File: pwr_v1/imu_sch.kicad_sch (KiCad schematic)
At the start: 5 parts, among them U4 LSM6DSLTR

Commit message: Schematic updated
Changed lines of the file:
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@@
+	)
+	(junction
+		(at 128.27 38.1)
+		(diameter 0)
+		(color 0 0 0 0)
 	)
 	(junction
@@
 	(junction
 		(at 67.31 55.88)
+		(diameter 0)
+		(color 0 0 0 0)
+	)
+	(junction
+		(at 53.34 55.88)
 		(diameter 0)
 		(color 0 0 0 0)
@@
 	)
 	(symbol
+		(lib_id "power:PWR_FLAG")
+		(at 53.34 55.88 90)
+		(unit 1)
+		(exclude_from_sim no)
+		(in_bom yes)
+		(on_board yes)
+		(dnp no)
+		(fields_autoplaced yes)
+		(property "Reference" "#FLG06"
+			(at 51.435 55.88 0)
+			(effects
+				(font
+					(size 1.27 1.27)
+				)
+				(hide yes)
+			)
+		)
+		(property "Value" "PWR_FLAG"
+			(at 49.53 55.8799 90)
+			(effects
+				(font
+					(size 1.27 1.27)
+				)
+				(justify left)
+			)
+		)
+		(property "Footprint" ""
+			(at 53.34 55.88 0)
+			(effects
+				(font
+					(size 1.27 1.27)
+				)
+				(hide yes)
+			)
+		)
+		(property "Datasheet" "~"
+			(at 53.34 55.88 0)
+			(effects
+				(font
+					(size 1.27 1.27)
+				)
+				(hide yes)
+			)
+		)
+		(property "Description" "Special symbol for telling ERC where power comes from"
+			(at 53.34 55.88 0)
+			(effects
+				(font
+					(size 1.27 1.27)
+				)
+				(hide yes)
+			)
+		)
+		(pin "1"
+		)
+		(instances
+			(project "pwr_v1"
+				(path "/42eee4f9-ea65-4e89-8296-df9554a24009/b4721251-ca72-44ff-8b38-c2b8be0e5ec8"
+					(reference "#FLG06")
+					(unit 1)
+				)
+			)
+		)
+	)
+	(symbol
 		(lib_id "imu:LSM6DSLTR")
 		(at 69.85 53.34 0)
@@
 					(unit 1)
 				)
+			)
+		)
+	)
+	(symbol
+		(lib_id "power:PWR_FLAG")
+		(at 128.27 38.1 270)
+		(unit 1)
+		(exclude_from_sim no)
+		(in_bom yes)
+		(on_board yes)
+		(dnp no)
+		(fields_autoplaced yes)
+		(property "Reference" "#FLG05"
+			(at 130.175 38.1 0)
+			(effects
+				(font
+					(size 1.27 1.27)
+				)
+				(hide yes)
+			)
+		)
+		(property "Value" "PWR_FLAG"
+			(at 132.08 38.0999 90)
+			(effects
+				(font
+					(size 1.27 1.27)
+				)
+				(justify left)
+			)
+		)
+		(property "Footprint" ""
+			(at 128.27 38.1 0)
+			(effects
+				(font
+					(size 1.27 1.27)
+				)
+				(hide yes)
+			)
+		)
+		(property "Datasheet" "~"
+			(at 128.27 38.1 0)
+			(effects
+				(font
+					(size 1.27 1.27)
+				)
+				(hide yes)
+			)
+		)
+		(property "Description" "Special symbol for telling ERC where power comes from"
+			(at 128.27 38.1 0)
+			(effects
+				(font
+					(size 1.27 1.27)
+				)
+				(hide yes)
+			)
+		)
+		(pin "1"
+		)
+		(instances
+			(project "pwr_v1"
+				(path "/42eee4f9-ea65-4e89-8296-df9554a24009/b4721251-ca72-44ff-8b38-c2b8be0e5ec8"
+					(reference "#FLG05")
+					(unit 1)
+				)

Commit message: Schematic and layout updated
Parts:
- C12, C13: footprint ceramic_cap:CAP_GRM155_MUR -> Capacitor_SMD:C_0402_1005Metric
- R2, R3: footprint res_1k:1206_PAN -> Resistor_SMD:R_0603_1608Metric
- U4: footprint (none) -> Package_LGA:LGA-14_3x2.5mm_P0.5mm_LayoutBorder3x4y

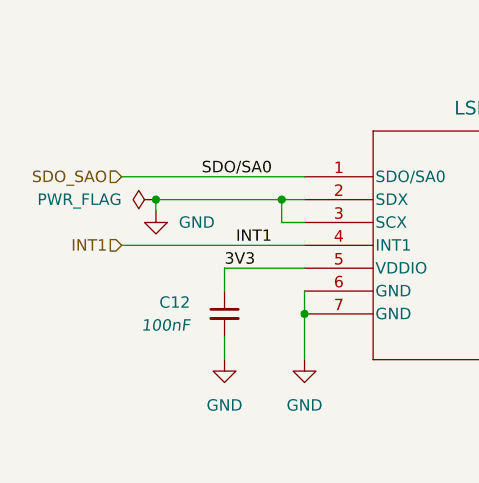
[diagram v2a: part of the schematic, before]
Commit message: Sch and Layout updated; Added batt sup ckt, placed and routed all motor drivers.
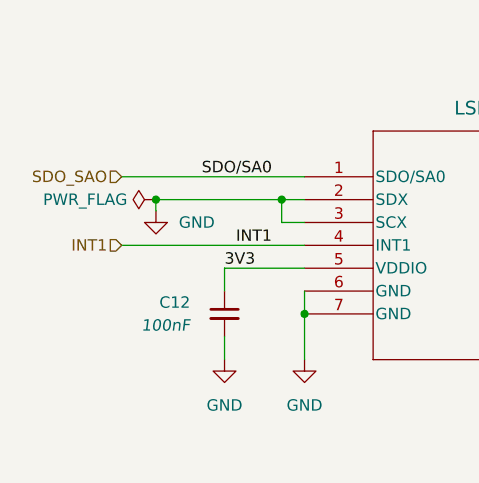
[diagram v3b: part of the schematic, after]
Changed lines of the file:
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@@
+	)
+	(junction
+		(at 53.34 55.88)
+		(diameter 0)
+		(color 0 0 0 0)
 	)
 	(junction
@@
 	(junction
 		(at 67.31 55.88)
-		(diameter 0)
-		(color 0 0 0 0)
-	)
-	(junction
-		(at 53.34 55.88)
 		(diameter 0)
 		(color 0 0 0 0)
@@
 	)
 	(symbol
-		(lib_id "power:PWR_FLAG")
-		(at 53.34 55.88 90)
-		(unit 1)
-		(exclude_from_sim no)
-		(in_bom yes)
-		(on_board yes)
-		(dnp no)
-		(fields_autoplaced yes)
-		(property "Reference" "#FLG06"
-			(at 51.435 55.88 0)
-			(effects
-				(font
-					(size 1.27 1.27)
-				)
-				(hide yes)
-			)
-		)
-		(property "Value" "PWR_FLAG"
-			(at 49.53 55.8799 90)
-			(effects
-				(font
-					(size 1.27 1.27)
-				)
-				(justify left)
-			)
-		)
-		(property "Footprint" ""
-			(at 53.34 55.88 0)
-			(effects
-				(font
-					(size 1.27 1.27)
-				)
-				(hide yes)
-			)
-		)
-		(property "Datasheet" "~"
-			(at 53.34 55.88 0)
-			(effects
-				(font
-					(size 1.27 1.27)
-				)
-				(hide yes)
-			)
-		)
-		(property "Description" "Special symbol for telling ERC where power comes from"
-			(at 53.34 55.88 0)
-			(effects
-				(font
-					(size 1.27 1.27)
-				)
-				(hide yes)
-			)
-		)
-		(pin "1"
-		)
-		(instances
-			(project "pwr_v1"
-				(path "/42eee4f9-ea65-4e89-8296-df9554a24009/b4721251-ca72-44ff-8b38-c2b8be0e5ec8"
-					(reference "#FLG06")
-					(unit 1)
-				)
-			)
-		)
-	)
-	(symbol
 		(lib_id "imu:LSM6DSLTR")
 		(at 69.85 53.34 0)
@@
 					(unit 1)
 				)
+			)
+		)
+	)
+	(symbol
+		(lib_id "power:PWR_FLAG")
+		(at 53.34 55.88 90)
+		(unit 1)
+		(exclude_from_sim no)
+		(in_bom yes)
+		(on_board yes)
+		(dnp no)
+		(fields_autoplaced yes)
+		(property "Reference" "#FLG04"
+			(at 51.435 55.88 0)
+			(effects
+				(font
+					(size 1.27 1.27)
+				)
+				(hide yes)
+			)
+		)
+		(property "Value" "PWR_FLAG"
+			(at 50.165 55.8799 90)
+			(effects
+				(font
+					(size 1.27 1.27)
+				)
+				(justify left)
+			)
+		)
+		(property "Footprint" ""
+			(at 53.34 55.88 0)
+			(effects
+				(font
+					(size 1.27 1.27)
+				)
+				(hide yes)
+			)
+		)
+		(property "Datasheet" "~"
+			(at 53.34 55.88 0)
+			(effects
+				(font
+					(size 1.27 1.27)
+				)
+				(hide yes)
+			)
+		)
+		(property "Description" "Special symbol for telling ERC where power comes from"
+			(at 53.34 55.88 0)
+			(effects
+				(font
+					(size 1.27 1.27)
+				)
+				(hide yes)
+			)
+		)
+		(pin "1"
+		)
+		(instances
+			(project "pwr_v1"
+				(path "/42eee4f9-ea65-4e89-8296-df9554a24009/b4721251-ca72-44ff-8b38-c2b8be0e5ec8"
+					(reference "#FLG04")
+					(unit 1)
+				)

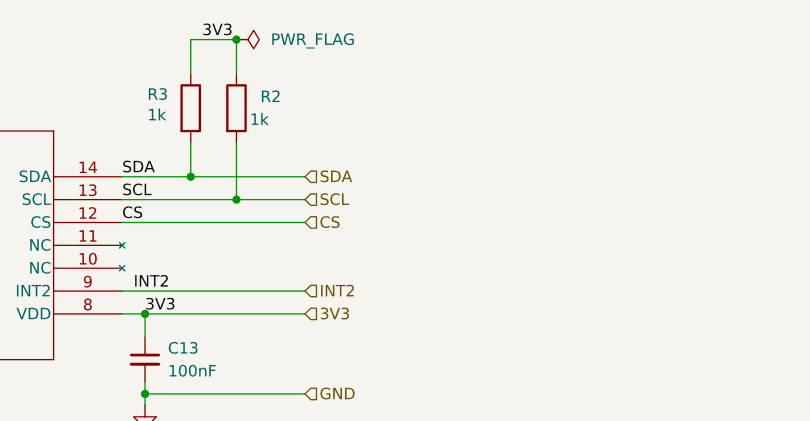
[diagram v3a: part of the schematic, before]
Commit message: Schematic updated; Layout updated; STM PinMappings file added
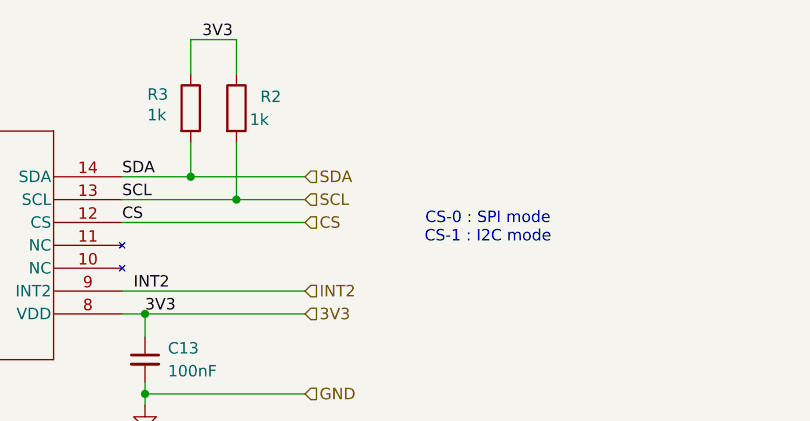
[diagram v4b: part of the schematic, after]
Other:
- note added: "CS-0 : SPI mode CS-1 : I2C mode"
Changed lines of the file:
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@@
-	)
-	(junction
-		(at 128.27 38.1)
-		(diameter 0)
-		(color 0 0 0 0)
 	)
 	(junction
@@
 			)
 			(justify left top)
+		)
+	)
+	(text "CS-0 : SPI mode\nCS-1 : I2C mode"
+		(exclude_from_sim no)
+		(at 156.21 59.055 0)
+		(effects
+			(font
+				(size 1.27 1.27)
+			)
 		)
 	)
@@
 					(unit 1)
 				)
-			)
-		)
-	)
-	(symbol
-		(lib_id "power:PWR_FLAG")
-		(at 128.27 38.1 270)
-		(unit 1)
-		(exclude_from_sim no)
-		(in_bom yes)
-		(on_board yes)
-		(dnp no)
-		(fields_autoplaced yes)
-		(property "Reference" "#FLG05"
-			(at 130.175 38.1 0)
-			(effects
-				(font
-					(size 1.27 1.27)
-				)
-				(hide yes)
-			)
-		)
-		(property "Value" "PWR_FLAG"
-			(at 132.08 38.0999 90)
-			(effects
-				(font
-					(size 1.27 1.27)
-				)
-				(justify left)
-			)
-		)
-		(property "Footprint" ""
-			(at 128.27 38.1 0)
-			(effects
-				(font
-					(size 1.27 1.27)
-				)
-				(hide yes)
-			)
-		)
-		(property "Datasheet" "~"
-			(at 128.27 38.1 0)
-			(effects
-				(font
-					(size 1.27 1.27)
-				)
-				(hide yes)
-			)
-		)
-		(property "Description" "Special symbol for telling ERC where power comes from"
-			(at 128.27 38.1 0)
-			(effects
-				(font
-					(size 1.27 1.27)
-				)
-				(hide yes)
-			)
-		)
-		(pin "1"
-		)
-		(instances
-			(project "pwr_v1"
-				(path "/42eee4f9-ea65-4e89-8296-df9554a24009/b4721251-ca72-44ff-8b38-c2b8be0e5ec8"
-					(reference "#FLG05")
-					(unit 1)
-				)

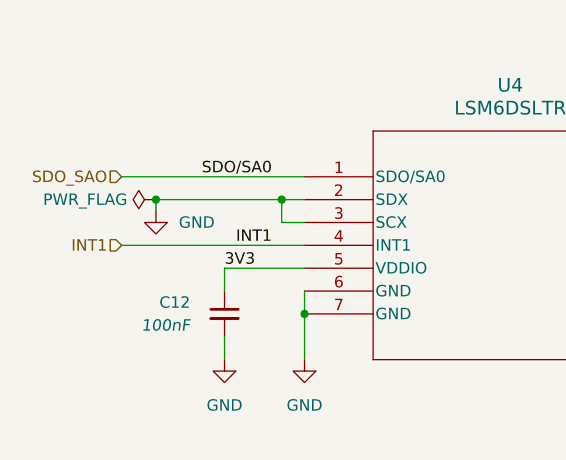
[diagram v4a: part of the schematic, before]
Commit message: Schematic and layout updated; Layout placement and routing completed
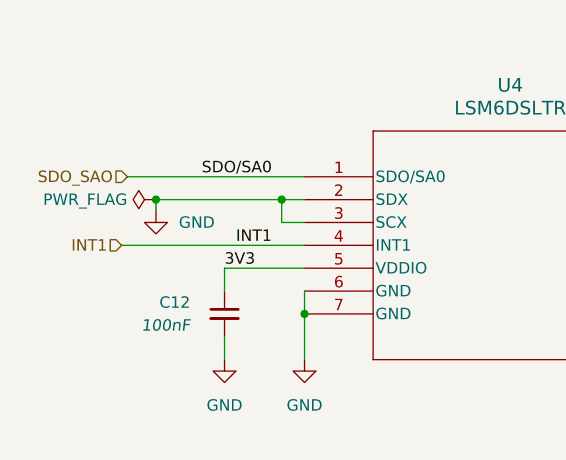
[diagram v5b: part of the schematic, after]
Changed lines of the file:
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@@
 	(wire
 		(pts
-			(xy 49.53 53.34) (xy 69.85 53.34)
+			(xy 50.165 53.34) (xy 69.85 53.34)
 		)
 		(stroke
@@
 	(hierarchical_label "SDO_SAO"
 		(shape input)
-		(at 49.53 53.34 180)
-		(fields_autoplaced yes)
-		(effects
+		(at 50.165 53.34 180)
+		(fields_autoplaced yes)
+		(effects

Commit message: Final PCB files sent for fab
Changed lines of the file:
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@@
 		)
 	)
-	(label "SDO{slash}SA0"
+	(label "SDO_SAO"
 		(at 58.42 53.34 0)
 		(fields_autoplaced yes)
@@
 	)
 	(symbol
+		(lib_name "GND_1")
 		(lib_id "power:GND")
 		(at 53.34 57.15 0)
@@
 			)
 		)
-		(property "Description" ""
+		(property "Description" "Power symbol creates a global label with name \"GND\" , ground"
 			(at 53.34 57.15 0)
 			(effects
@@
 			)
 		)
-		(property "Description" ""
+		(property "Description" "Power symbol creates a global label with name \"GND\" , ground"
 			(at 60.96 73.66 0)
 			(effects
@@
 			)
 		)
-		(property "Description" ""
+		(property "Description" "Power symbol creates a global label with name \"GND\" , ground"
 			(at 69.85 73.66 0)
 			(effects
@@
 			)
 		)
-		(property "Description" ""
+		(property "Description" "Power symbol creates a global label with name \"GND\" , ground"
 			(at 118.11 78.74 0)
 			(effects

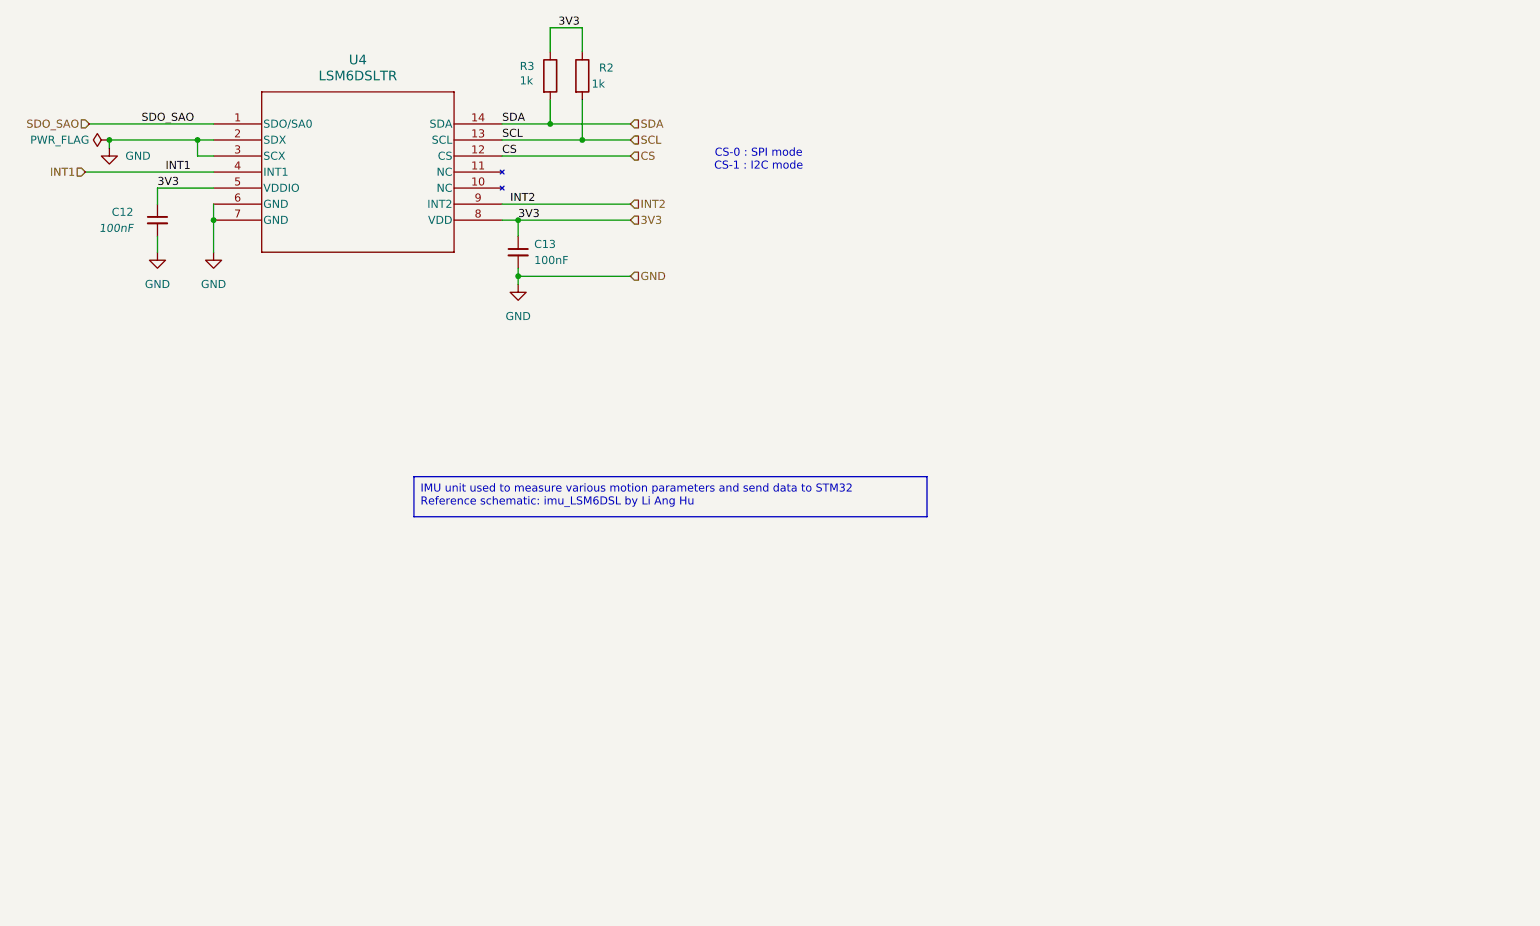
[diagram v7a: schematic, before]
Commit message: File structure enhanced.
Added uniform titleblocks and 3D renders for easier view, file cleanups.
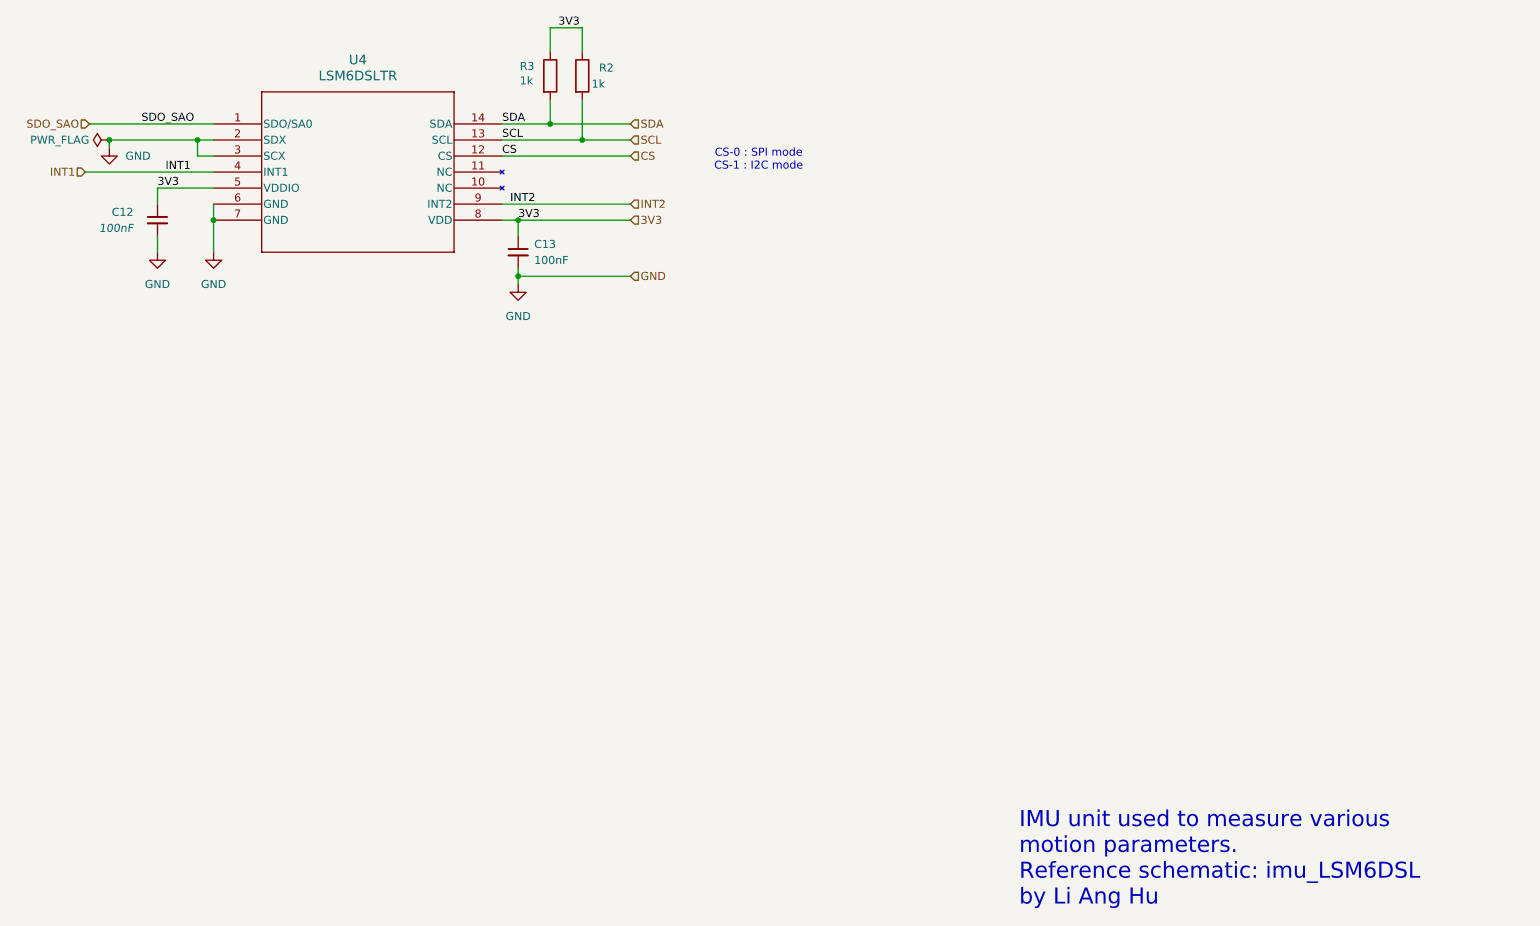
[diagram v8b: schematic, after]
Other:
- title: (none) -> Power board
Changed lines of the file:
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@@
 (kicad_sch
-	(version 20231120)
+	(version 20250114)
 	(generator "eeschema")
-	(generator_version "8.0")
-	(paper "A5")
+	(generator_version "9.0")
+	(paper "A4")
+	(title_block
+		(title "Power board")
+		(date "06-08-2024")
+		(rev "1")
+	)
+	(text "CS-0 : SPI mode\nCS-1 : I2C mode"
+		(exclude_from_sim no)
+		(at 156.21 59.055 0)
+		(effects
+			(font
+				(size 1.27 1.27)
+			)
+		)
+	)
+	(text_box "IMU unit used to measure various motion parameters.\nReference schematic: imu_LSM6DSL by Li Ang Hu"
+		(exclude_from_sim no)
+		(at 195.58 160.02 0)
+		(size 78.105 12.7)
+		(margins 1.905 1.905 1.905 1.905)
+		(stroke
+			(width -0.0001)
+			(type solid)
+		)
+		(fill
+			(type none)
+		)
+		(effects
+			(font
+				(size 2.54 2.54)
+			)
+			(justify left top)
+		)
+	)
 	(junction
 		(at 118.11 68.58)
@@
 		)
 	)
-	(text_box "IMU unit used to measure various motion parameters and send data to STM32\nReference schematic: imu_LSM6DSL by Li Ang Hu"
-		(exclude_from_sim no)
-		(at 101.6 109.22 0)
-		(size 81.28 6.35)
-		(stroke
-			(width 0)
-			(type default)
-		)
-		(fill
-			(type none)
-		)
-		(effects
-			(font
-				(size 1.27 1.27)
-			)
-			(justify left top)
-		)
-	)
-	(text "CS-0 : SPI mode\nCS-1 : I2C mode"
-		(exclude_from_sim no)
-		(at 156.21 59.055 0)
-		(effects
-			(font
-				(size 1.27 1.27)
-			)
-		)
-	)
 	(label "3V3"
 		(at 118.11 68.58 0)
-		(fields_autoplaced yes)
 		(effects
 			(font
@@
 	(label "INT2"
 		(at 116.84 66.04 0)
-		(fields_autoplaced yes)
 		(effects
 			(font
@@
 	(label "3V3"
 		(at 124.46 38.1 0)
-		(fields_autoplaced yes)
 		(effects
 			(font
@@
 	(label "SDO_SAO"
 		(at 58.42 53.34 0)
-		(fields_autoplaced yes)
 		(effects
 			(font
@@
 	(label "SCL"
 		(at 115.57 55.88 0)
-		(fields_autoplaced yes)
 		(effects
 			(font
@@
 	(label "3V3"
 		(at 60.96 63.5 0)
-		(fields_autoplaced yes)
 		(effects
 			(font
@@
 	(label "SDA"
 		(at 115.57 53.34 0)
-		(fields_autoplaced yes)
 		(effects
 			(font
@@
 	(label "INT1"
 		(at 62.23 60.96 0)
-		(fields_autoplaced yes)
 		(effects
 			(font
@@
 	(label "CS"
 		(at 115.57 58.42 0)
-		(fields_autoplaced yes)
 		(effects
 			(font
@@
 		(shape input)
 		(at 135.89 58.42 0)
-		(fields_autoplaced yes)
 		(effects
 			(font
@@
 		(shape input)
 		(at 135.89 66.04 0)
-		(fields_autoplaced yes)
 		(effects
 			(font
@@
 		(shape input)
 		(at 50.165 53.34 180)
-		(fields_autoplaced yes)
 		(effects
 			(font
@@
 		(shape input)
 		(at 49.53 60.96 180)
-		(fields_autoplaced yes)
 		(effects
 			(font
@@
 		(shape input)
 		(at 135.89 55.88 0)
-		(fields_autoplaced yes)
 		(effects
 			(font
@@
 		(shape input)
 		(at 135.89 68.58 0)
-		(fields_autoplaced yes)
 		(effects
 			(font
@@
 		(shape input)
 		(at 135.89 53.34 0)
-		(fields_autoplaced yes)
 		(effects
 			(font
@@
 		(shape input)
 		(at 135.89 77.47 0)
-		(fields_autoplaced yes)
 		(effects
 			(font
@@
 		)
 	)
+	(embedded_fonts no)
+	(embedded_files
+		(file
+			(name "SeeGoals.kicad_wks")
+			(type worksheet)
+			(data |KLUv/WBWCEUVAKZhaSDwGD3QEeyM1Nkm1gfAFENB192U/Uu5smaFjYXFwbleVGAAXQBiAJ3fHl7X
+				Y9LV3cOctHvfXWn3EChzOV9nEL8kT/9g0GBnlB/qX0ZhnUGDjfPxKoc9hXsBAAgISqaOQxm3y3Pl
+				D3vA0vV898uxxiCDNuesVNLXO4ccnwqAgCAcoTzf9fKoENH+NmmcG61b1B6zWMxqi9MsGh5uk8lE
+				WIRX4H4bnHMVx11j71Wf3EOTyNKfCxW1L7uuk7MWAF3vz3xLP9yla17fU7h33cpq6UurSnFPZ/r9
+				4hJ++Z/GHGu+vQ7KD5SjLCrcJOLIDi+Dt+c30KfUblic9K1mo9wmmogG7Fnz5e8YhzK0alGbn2ED
+				RGvwRT5wd09nzWKdNcLhMCeMuf67XpZc3zUmkbaXYVqsP7OKJZLBcBxPY8GISFgEm8lIqUzYAYFh
+				5G2w+/441P/Tps3vY7NWardYp+6EXu6725hfRBx/CMG7Hxhfr9K3RNqMLRHrJyxGE1rUvkqaQyHp
+				8htq/FX1/C1eoer+wxqUQ9ygWcQgmsVFw3GQjJQxMbMsizNqoPE4ZRwaqlGQNhnGUISIGbtuzyGn
+				lKLOBfFKGKkDMleBRYmd+5lzd8a/EMWXlwELeZPPxs5h2q26xzeF3cWJrdCkNHThwclSRVgc7Dxs
+				MDMBL5YFRtvnhSGIHvsw9DvTX0LDM7kiJLLMgQAug8cycePhfwgg9p0jKCmmgSwuO10DIfREMvJw
+				LLj/XY/Uc30G6agTD3QoENPIaa/cRm4toMWW/gBBiO5x6hcVBV46gAt257j3s/hpM5Qllp35xv/E
+				NrWcdAgCmKGamAagRtgP3ENBfATG+0F8zQAN0JLmhSfpliXkbEcKm+yAvU9vmyZDF97SNzwfcQcZ
+				bgE1BqEK|
+			)
+			(checksum "714487A7A475B68BB3B3E7DC8D393DDF")
+		)
+	)
